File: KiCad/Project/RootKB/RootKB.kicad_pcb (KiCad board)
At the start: 2 copper layers, 137.4 x 107.4 mm, 70 parts, among them J1 OLED-128x32, SW1 Switch, U1 Arduino_Pro_Micro, U2 TRRS

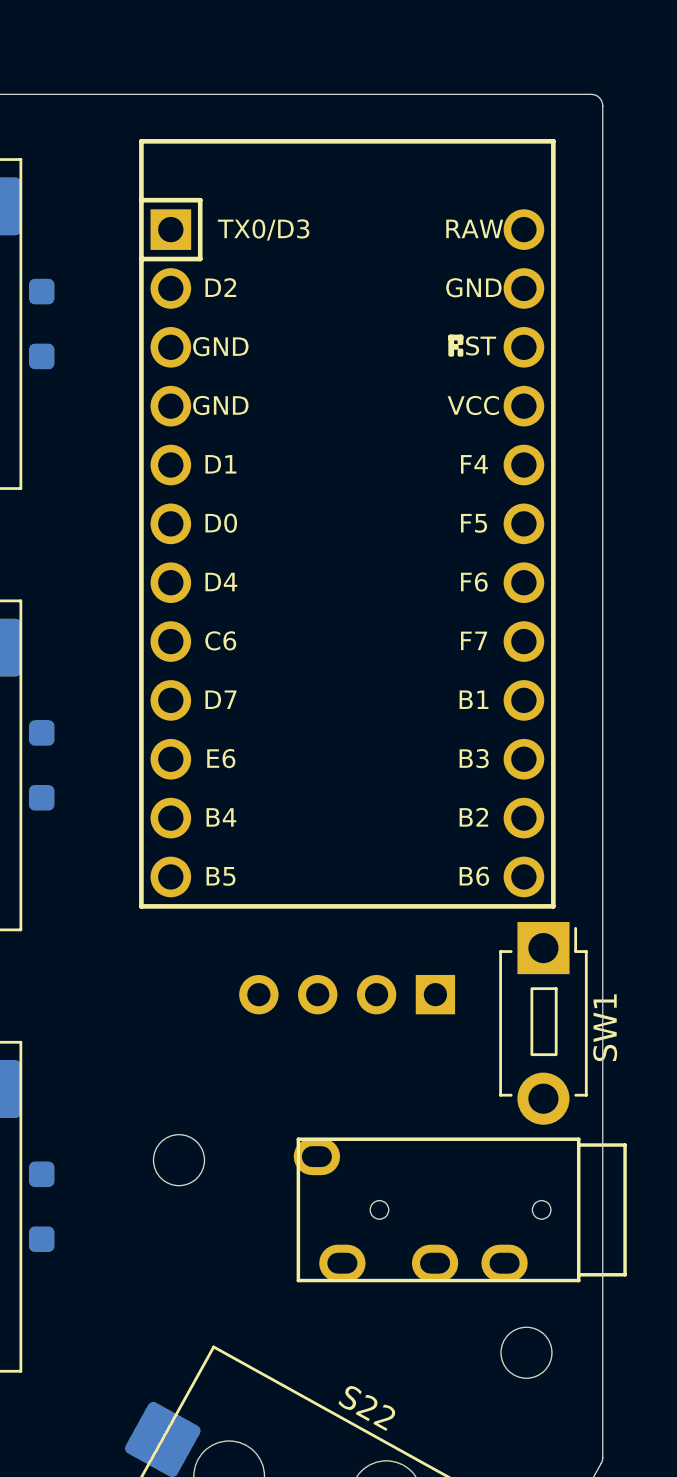
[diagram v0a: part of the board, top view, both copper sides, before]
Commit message: adjust for larger arduino pro micro (Type C)
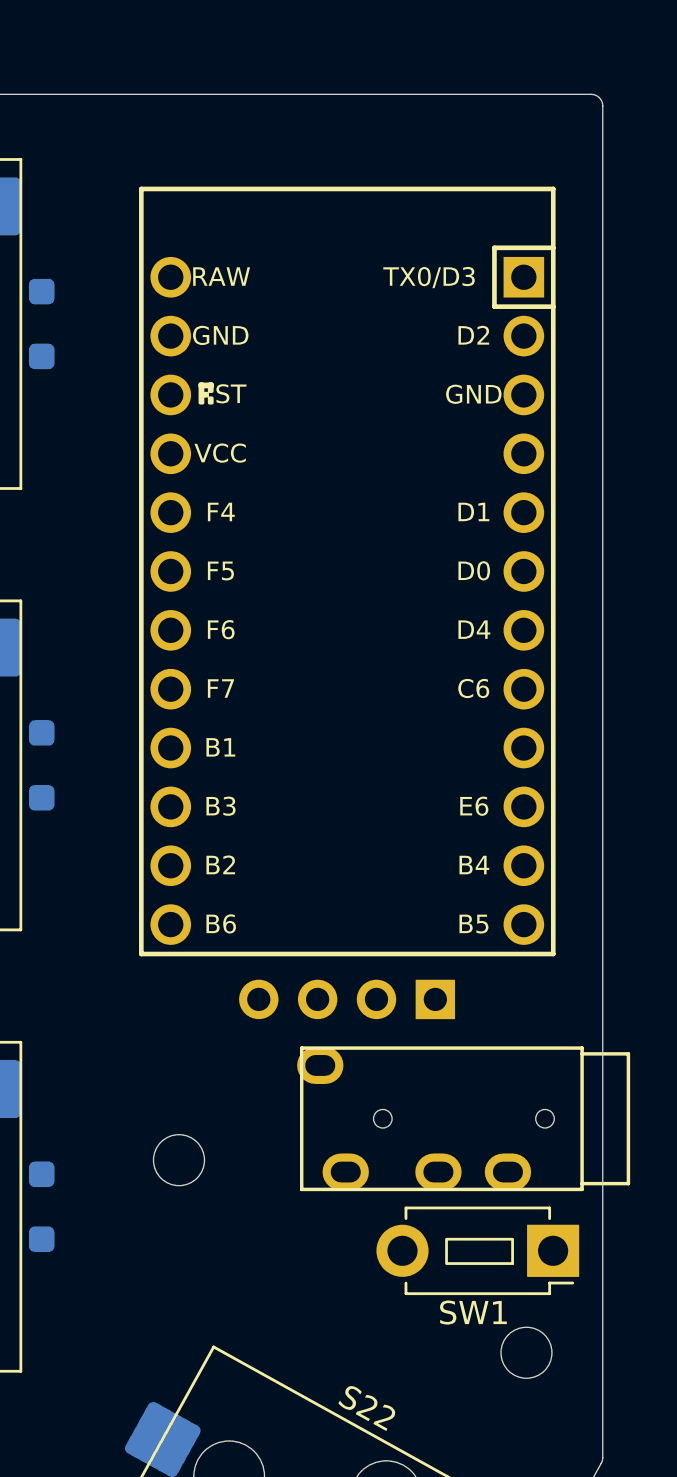
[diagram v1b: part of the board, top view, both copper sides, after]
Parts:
- U1: moved to B.Cu
- moved SW1 13.1 mm to (211.0, 101.9), turned to 180 degrees
- moved U2 3.94 mm to (212.3, 96.2)
- moved U1 2.06 mm to (202.2, 73.9), turned to 180 degrees
- moved J1 0.21 mm to (196.2, 92.7)

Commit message: add right side
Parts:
- removed the D1 at (93.7, 61.9)
- removed the D10 at (150.9, 71.4)
- removed the D11 at (169.9, 76.2)
- removed the D12 at (189.0, 81.0)
- removed the D13 at (93.7, 100.0)
- removed the D14 at (112.8, 100.0)
- removed the D15 at (131.8, 95.2)
- removed the D16 at (150.9, 90.5)
- removed the D17 at (169.9, 95.2)
- removed the D18 at (189.0, 100.0)
- removed the D19 at (161.2, 121.9)
- removed the D2 at (112.8, 61.9)
- removed the D20 at (179.1, 129.1)
- removed the D21 at (195.8, 138.2)
- removed the D22 at (206.1, 119.7)
- removed the D3 at (131.8, 57.1)
- removed the D4 at (150.9, 52.4)
- removed the D5 at (169.9, 57.1)
- removed the D6 at (189.0, 61.9)
- removed the D7 at (93.7, 81.0)
- removed the D8 at (112.8, 81.0)
- removed the D9 at (131.8, 76.2)
- removed the J1 at (196.2, 92.7)
- removed the LED1 at (85.7, 67.0)
- removed the LED10 at (142.9, 76.5)
- removed the LED11 at (161.9, 81.3)
- removed the LED12 at (181.0, 86.0)
- removed the LED13 at (85.7, 105.1)
- removed the LED14 at (104.8, 105.1)
- removed the LED15 at (123.8, 100.3)
- removed the LED16 at (142.9, 95.6)
- removed the LED17 at (161.9, 100.3)
- removed the LED18 at (181.0, 105.1)
- removed the LED19 at (151.8, 122.5)
- removed the LED2 at (104.8, 67.0)
- removed the LED20 at (169.7, 129.6)
- removed the LED21 at (186.3, 138.9)
- removed the LED22 at (196.7, 120.2)
- removed the LED3 at (123.8, 62.2)
- removed the LED4 at (142.9, 57.5)
- removed the LED5 at (161.9, 62.2)
- removed the LED6 at (181.0, 67.0)
- removed the LED7 at (85.7, 86.0)
- removed the LED8 at (104.8, 86.0)
- removed the LED9 at (123.8, 81.3)
- removed the S1 at (85.7, 61.9)
- removed the S10 at (142.9, 71.4)
- removed the S11 at (161.9, 76.2)
- removed the S12 at (181.0, 81.0)
- removed the S13 at (85.7, 100.0)
- removed the S14 at (104.8, 100.0)
- removed the S15 at (123.8, 95.2)
- removed the S16 at (142.9, 90.5)
- removed the S17 at (161.9, 95.2)
- removed the S18 at (181.0, 100.0)
- removed the S19 at (154.3, 118.1)
- removed the S2 at (104.8, 61.9)
- removed the S20 at (172.1, 125.2)
- removed the S21 at (188.8, 134.4)
- removed the S22 at (199.2, 115.7)
- removed the S3 at (123.8, 57.1)
- removed the S4 at (142.9, 52.4)
- removed the S5 at (161.9, 57.1)
- removed the S6 at (181.0, 61.9)
- removed the S7 at (85.7, 81.0)
- removed the S8 at (104.8, 81.0)
- removed the S9 at (123.8, 76.2)
- removed the SW1 at (211.0, 101.9)
- removed the U1 at (202.2, 73.9)
- removed the U2 at (212.3, 96.2)
- added D1: Diode, Diode_SMD:D_SOD-123F, B.Cu at (348.4, 105.7)
- added D1: Diode, Diode_SMD:D_SOD-123F, B.Cu at (74.9, 104.9)
- added D10: Diode, Diode_SMD:D_SOD-123F, B.Cu at (291.2, 115.2)
- added D10: Diode, Diode_SMD:D_SOD-123F, B.Cu at (132.1, 114.4)
- added D11: Diode, Diode_SMD:D_SOD-123F, B.Cu at (272.2, 120.0)
- added D11: Diode, Diode_SMD:D_SOD-123F, B.Cu at (151.1, 119.2)
- added D12: Diode, Diode_SMD:D_SOD-123F, B.Cu at (170.2, 123.9)
- added D12: Diode, Diode_SMD:D_SOD-123F, B.Cu at (253.1, 124.7)
- added D13: Diode, Diode_SMD:D_SOD-123F, B.Cu at (74.9, 143.0)
- added D13: Diode, Diode_SMD:D_SOD-123F, B.Cu at (348.4, 143.8)
- added D14: Diode, Diode_SMD:D_SOD-123F, B.Cu at (329.3, 143.8)
- added D14: Diode, Diode_SMD:D_SOD-123F, B.Cu at (94.0, 143.0)
- added D15: Diode, Diode_SMD:D_SOD-123F, B.Cu at (113.0, 138.2)
- added D15: Diode, Diode_SMD:D_SOD-123F, B.Cu at (310.3, 139.0)
- added D16: Diode, Diode_SMD:D_SOD-123F, B.Cu at (291.2, 134.2)
- added D16: Diode, Diode_SMD:D_SOD-123F, B.Cu at (132.1, 133.5)
- added D17: Diode, Diode_SMD:D_SOD-123F, B.Cu at (272.2, 139.0)
- added D17: Diode, Diode_SMD:D_SOD-123F, B.Cu at (151.1, 138.2)
- added D18: Diode, Diode_SMD:D_SOD-123F, B.Cu at (170.2, 143.0)
- added D18: Diode, Diode_SMD:D_SOD-123F, B.Cu at (253.1, 143.8)
- added D19: Diode, Diode_SMD:D_SOD-123F, B.Cu at (278.9, 157.8)
- added D19: Diode, Diode_SMD:D_SOD-123F, B.Cu at (142.4, 164.9)
- added D2: Diode, Diode_SMD:D_SOD-123F, B.Cu at (329.3, 105.7)
- added D2: Diode, Diode_SMD:D_SOD-123F, B.Cu at (94.0, 104.9)
- added D20: Diode, Diode_SMD:D_SOD-123F, B.Cu at (160.3, 172.0)
- added D20: Diode, Diode_SMD:D_SOD-123F, B.Cu at (261.0, 165.0)
- added D21: Diode, Diode_SMD:D_SOD-123F, B.Cu at (244.4, 174.1)
- added D21: Diode, Diode_SMD:D_SOD-123F, B.Cu at (177.0, 181.2)
- added D22: Diode, Diode_SMD:D_SOD-123F, B.Cu at (187.3, 162.6)
- added D22: Diode, Diode_SMD:D_SOD-123F, B.Cu at (234.0, 155.5)
- added D3: Diode, Diode_SMD:D_SOD-123F, B.Cu at (310.3, 100.9)
- added D3: Diode, Diode_SMD:D_SOD-123F, B.Cu at (113.0, 100.1)
- added D4: Diode, Diode_SMD:D_SOD-123F, B.Cu at (291.2, 96.2)
- added D4: Diode, Diode_SMD:D_SOD-123F, B.Cu at (132.1, 95.4)
- added D5: Diode, Diode_SMD:D_SOD-123F, B.Cu at (272.2, 100.9)
- added D5: Diode, Diode_SMD:D_SOD-123F, B.Cu at (151.1, 100.1)
- added D6: Diode, Diode_SMD:D_SOD-123F, B.Cu at (170.2, 104.9)
- added D6: Diode, Diode_SMD:D_SOD-123F, B.Cu at (253.1, 105.7)
- added D7: Diode, Diode_SMD:D_SOD-123F, B.Cu at (74.9, 123.9)
- added D7: Diode, Diode_SMD:D_SOD-123F, B.Cu at (348.4, 124.7)
- added D8: Diode, Diode_SMD:D_SOD-123F, B.Cu at (329.3, 124.7)
- added D8: Diode, Diode_SMD:D_SOD-123F, B.Cu at (94.0, 123.9)
- added D9: Diode, Diode_SMD:D_SOD-123F, B.Cu at (113.0, 119.2)
- added D9: Diode, Diode_SMD:D_SOD-123F, B.Cu at (310.3, 120.0)
- added J1: OLED-128x32, display:OLED-128x32-cutout, F.Cu at (217.8, 136.4)
- added J1: OLED-128x32, display:OLED-128x32-cutout, F.Cu at (177.4, 135.6)
- added LED1: MX_SK6812MINI-E, PCM_marbastlib-mx:LED_MX_6028R, B.Cu at (340.3, 110.8)
- added LED1: MX_SK6812MINI-E, PCM_marbastlib-mx:LED_MX_6028R, B.Cu at (66.9, 110.0)
- added LED10: MX_SK6812MINI-E, PCM_marbastlib-mx:LED_MX_6028R, B.Cu at (124.1, 119.5)
- added LED10: MX_SK6812MINI-E, PCM_marbastlib-mx:LED_MX_6028R, B.Cu at (283.1, 120.3)
- added LED11: MX_SK6812MINI-E, PCM_marbastlib-mx:LED_MX_6028R, B.Cu at (143.1, 124.2)
- added LED11: MX_SK6812MINI-E, PCM_marbastlib-mx:LED_MX_6028R, B.Cu at (264.1, 125.0)
- added LED12: MX_SK6812MINI-E, PCM_marbastlib-mx:LED_MX_6028R, B.Cu at (162.2, 129.0)
- added LED12: MX_SK6812MINI-E, PCM_marbastlib-mx:LED_MX_6028R, B.Cu at (245.0, 129.8)
- added LED13: MX_SK6812MINI-E, PCM_marbastlib-mx:LED_MX_6028R, B.Cu at (66.9, 148.1)
- added LED13: MX_SK6812MINI-E, PCM_marbastlib-mx:LED_MX_6028R, B.Cu at (340.3, 148.9)
- added LED14: MX_SK6812MINI-E, PCM_marbastlib-mx:LED_MX_6028R, B.Cu at (321.2, 148.9)
- added LED14: MX_SK6812MINI-E, PCM_marbastlib-mx:LED_MX_6028R, B.Cu at (86.0, 148.1)
- added LED15: MX_SK6812MINI-E, PCM_marbastlib-mx:LED_MX_6028R, B.Cu at (105.0, 143.3)
- added LED15: MX_SK6812MINI-E, PCM_marbastlib-mx:LED_MX_6028R, B.Cu at (302.2, 144.1)
- added LED16: MX_SK6812MINI-E, PCM_marbastlib-mx:LED_MX_6028R, B.Cu at (124.1, 138.5)
- added LED16: MX_SK6812MINI-E, PCM_marbastlib-mx:LED_MX_6028R, B.Cu at (283.1, 139.3)
- added LED17: MX_SK6812MINI-E, PCM_marbastlib-mx:LED_MX_6028R, B.Cu at (264.1, 144.1)
- added LED17: MX_SK6812MINI-E, PCM_marbastlib-mx:LED_MX_6028R, B.Cu at (143.1, 143.3)
- added LED18: MX_SK6812MINI-E, PCM_marbastlib-mx:LED_MX_6028R, B.Cu at (245.0, 148.9)
- added LED18: MX_SK6812MINI-E, PCM_marbastlib-mx:LED_MX_6028R, B.Cu at (162.2, 148.1)
- added LED19: MX_SK6812MINI-E, PCM_marbastlib-mx:LED_MX_6028R, B.Cu at (133.1, 165.5)
- added LED19: MX_SK6812MINI-E, PCM_marbastlib-mx:LED_MX_6028R, B.Cu at (274.2, 166.3)
- added LED2: MX_SK6812MINI-E, PCM_marbastlib-mx:LED_MX_6028R, B.Cu at (321.2, 110.8)
- added LED2: MX_SK6812MINI-E, PCM_marbastlib-mx:LED_MX_6028R, B.Cu at (86.0, 110.0)
- added LED20: MX_SK6812MINI-E, PCM_marbastlib-mx:LED_MX_6028R, B.Cu at (150.9, 172.6)
- added LED20: MX_SK6812MINI-E, PCM_marbastlib-mx:LED_MX_6028R, B.Cu at (256.3, 173.4)
- added LED21: MX_SK6812MINI-E, PCM_marbastlib-mx:LED_MX_6028R, B.Cu at (239.7, 182.6)
- added LED21: MX_SK6812MINI-E, PCM_marbastlib-mx:LED_MX_6028R, B.Cu at (167.5, 181.8)
- added LED22: MX_SK6812MINI-E, PCM_marbastlib-mx:LED_MX_6028R, B.Cu at (177.9, 163.1)
- added LED22: MX_SK6812MINI-E, PCM_marbastlib-mx:LED_MX_6028R, B.Cu at (229.3, 163.9)
- added LED3: MX_SK6812MINI-E, PCM_marbastlib-mx:LED_MX_6028R, B.Cu at (302.2, 106.0)
- added LED3: MX_SK6812MINI-E, PCM_marbastlib-mx:LED_MX_6028R, B.Cu at (105.0, 105.2)
- added LED4: MX_SK6812MINI-E, PCM_marbastlib-mx:LED_MX_6028R, B.Cu at (124.1, 100.4)
- added LED4: MX_SK6812MINI-E, PCM_marbastlib-mx:LED_MX_6028R, B.Cu at (283.1, 101.2)
- added LED5: MX_SK6812MINI-E, PCM_marbastlib-mx:LED_MX_6028R, B.Cu at (143.1, 105.2)
- added LED5: MX_SK6812MINI-E, PCM_marbastlib-mx:LED_MX_6028R, B.Cu at (264.1, 106.0)
- added LED6: MX_SK6812MINI-E, PCM_marbastlib-mx:LED_MX_6028R, B.Cu at (245.0, 110.8)
- added LED6: MX_SK6812MINI-E, PCM_marbastlib-mx:LED_MX_6028R, B.Cu at (162.2, 110.0)
- added LED7: MX_SK6812MINI-E, PCM_marbastlib-mx:LED_MX_6028R, B.Cu at (340.3, 129.8)
- added LED7: MX_SK6812MINI-E, PCM_marbastlib-mx:LED_MX_6028R, B.Cu at (66.9, 129.0)
- added LED8: MX_SK6812MINI-E, PCM_marbastlib-mx:LED_MX_6028R, B.Cu at (86.0, 129.0)
- added LED8: MX_SK6812MINI-E, PCM_marbastlib-mx:LED_MX_6028R, B.Cu at (321.2, 129.8)
- added LED9: MX_SK6812MINI-E, PCM_marbastlib-mx:LED_MX_6028R, B.Cu at (302.2, 125.0)
- added LED9: MX_SK6812MINI-E, PCM_marbastlib-mx:LED_MX_6028R, B.Cu at (105.0, 124.2)
- added S1: Keyswitch, PCM_Switch_Keyboard_Hotswap_Kailh:SW_Hotswap_Kailh_MX_1.00u, F.Cu at (66.9, 104.9)
- added S1: Keyswitch, PCM_Switch_Keyboard_Hotswap_Kailh:SW_Hotswap_Kailh_MX_1.00u, F.Cu at (340.3, 105.7)
- added S10: Keyswitch, PCM_Switch_Keyboard_Hotswap_Kailh:SW_Hotswap_Kailh_MX_1.00u, F.Cu at (283.1, 115.2)
- added S10: Keyswitch, PCM_Switch_Keyboard_Hotswap_Kailh:SW_Hotswap_Kailh_MX_1.00u, F.Cu at (124.1, 114.4)
- added S11: Keyswitch, PCM_Switch_Keyboard_Hotswap_Kailh:SW_Hotswap_Kailh_MX_1.00u, F.Cu at (264.1, 120.0)
- added S11: Keyswitch, PCM_Switch_Keyboard_Hotswap_Kailh:SW_Hotswap_Kailh_MX_1.00u, F.Cu at (143.1, 119.2)
- added S12: Keyswitch, PCM_Switch_Keyboard_Hotswap_Kailh:SW_Hotswap_Kailh_MX_1.00u, F.Cu at (245.0, 124.7)
- added S12: Keyswitch, PCM_Switch_Keyboard_Hotswap_Kailh:SW_Hotswap_Kailh_MX_1.00u, F.Cu at (162.2, 123.9)
- added S13: Keyswitch, PCM_Switch_Keyboard_Hotswap_Kailh:SW_Hotswap_Kailh_MX_1.00u, F.Cu at (66.9, 143.0)
- added S13: Keyswitch, PCM_Switch_Keyboard_Hotswap_Kailh:SW_Hotswap_Kailh_MX_1.00u, F.Cu at (340.3, 143.8)
- added S14: Keyswitch, PCM_Switch_Keyboard_Hotswap_Kailh:SW_Hotswap_Kailh_MX_1.00u, F.Cu at (321.2, 143.8)
- added S14: Keyswitch, PCM_Switch_Keyboard_Hotswap_Kailh:SW_Hotswap_Kailh_MX_1.00u, F.Cu at (86.0, 143.0)
- added S15: Keyswitch, PCM_Switch_Keyboard_Hotswap_Kailh:SW_Hotswap_Kailh_MX_1.00u, F.Cu at (105.0, 138.2)
- added S15: Keyswitch, PCM_Switch_Keyboard_Hotswap_Kailh:SW_Hotswap_Kailh_MX_1.00u, F.Cu at (302.2, 139.0)
- added S16: Keyswitch, PCM_Switch_Keyboard_Hotswap_Kailh:SW_Hotswap_Kailh_MX_1.00u, F.Cu at (283.1, 134.2)
- added S16: Keyswitch, PCM_Switch_Keyboard_Hotswap_Kailh:SW_Hotswap_Kailh_MX_1.00u, F.Cu at (124.1, 133.5)
- added S17: Keyswitch, PCM_Switch_Keyboard_Hotswap_Kailh:SW_Hotswap_Kailh_MX_1.00u, F.Cu at (143.1, 138.2)
- added S17: Keyswitch, PCM_Switch_Keyboard_Hotswap_Kailh:SW_Hotswap_Kailh_MX_1.00u, F.Cu at (264.1, 139.0)
- added S18: Keyswitch, PCM_Switch_Keyboard_Hotswap_Kailh:SW_Hotswap_Kailh_MX_1.00u, F.Cu at (245.0, 143.8)
- added S18: Keyswitch, PCM_Switch_Keyboard_Hotswap_Kailh:SW_Hotswap_Kailh_MX_1.00u, F.Cu at (162.2, 143.0)
- added S19: Keyswitch, PCM_Switch_Keyboard_Hotswap_Kailh:SW_Hotswap_Kailh_MX_1.00u, F.Cu at (271.7, 161.8)
- added S19: Keyswitch, PCM_Switch_Keyboard_Hotswap_Kailh:SW_Hotswap_Kailh_MX_1.00u, F.Cu at (135.5, 161.0)
- added S2: Keyswitch, PCM_Switch_Keyboard_Hotswap_Kailh:SW_Hotswap_Kailh_MX_1.00u, F.Cu at (321.2, 105.7)
- added S2: Keyswitch, PCM_Switch_Keyboard_Hotswap_Kailh:SW_Hotswap_Kailh_MX_1.00u, F.Cu at (86.0, 104.9)
- added S20: Keyswitch, PCM_Switch_Keyboard_Hotswap_Kailh:SW_Hotswap_Kailh_MX_1.25u_90deg, F.Cu at (253.9, 169.0)
- added S20: Keyswitch, PCM_Switch_Keyboard_Hotswap_Kailh:SW_Hotswap_Kailh_MX_1.25u_90deg, F.Cu at (153.3, 168.2)
- added S21: Keyswitch, PCM_Switch_Keyboard_Hotswap_Kailh:SW_Hotswap_Kailh_MX_1.25u_90deg, F.Cu at (237.2, 178.2)
- added S21: Keyswitch, PCM_Switch_Keyboard_Hotswap_Kailh:SW_Hotswap_Kailh_MX_1.25u_90deg, F.Cu at (170.0, 177.4)
- added S22: Keyswitch, PCM_Switch_Keyboard_Hotswap_Kailh:SW_Hotswap_Kailh_MX_1.00u, F.Cu at (226.8, 159.5)
- added S22: Keyswitch, PCM_Switch_Keyboard_Hotswap_Kailh:SW_Hotswap_Kailh_MX_1.00u, F.Cu at (180.4, 158.7)
- added S3: Keyswitch, PCM_Switch_Keyboard_Hotswap_Kailh:SW_Hotswap_Kailh_MX_1.00u, F.Cu at (302.2, 100.9)
- added S3: Keyswitch, PCM_Switch_Keyboard_Hotswap_Kailh:SW_Hotswap_Kailh_MX_1.00u, F.Cu at (105.0, 100.1)
- added S4: Keyswitch, PCM_Switch_Keyboard_Hotswap_Kailh:SW_Hotswap_Kailh_MX_1.00u, F.Cu at (124.1, 95.4)
- added S4: Keyswitch, PCM_Switch_Keyboard_Hotswap_Kailh:SW_Hotswap_Kailh_MX_1.00u, F.Cu at (283.1, 96.2)
- added S5: Keyswitch, PCM_Switch_Keyboard_Hotswap_Kailh:SW_Hotswap_Kailh_MX_1.00u, F.Cu at (264.1, 100.9)
- added S5: Keyswitch, PCM_Switch_Keyboard_Hotswap_Kailh:SW_Hotswap_Kailh_MX_1.00u, F.Cu at (143.1, 100.1)
- added S6: Keyswitch, PCM_Switch_Keyboard_Hotswap_Kailh:SW_Hotswap_Kailh_MX_1.00u, F.Cu at (245.0, 105.7)
- added S6: Keyswitch, PCM_Switch_Keyboard_Hotswap_Kailh:SW_Hotswap_Kailh_MX_1.00u, F.Cu at (162.2, 104.9)
- added S7: Keyswitch, PCM_Switch_Keyboard_Hotswap_Kailh:SW_Hotswap_Kailh_MX_1.00u, F.Cu at (340.3, 124.7)
- added S7: Keyswitch, PCM_Switch_Keyboard_Hotswap_Kailh:SW_Hotswap_Kailh_MX_1.00u, F.Cu at (66.9, 123.9)
- added S8: Keyswitch, PCM_Switch_Keyboard_Hotswap_Kailh:SW_Hotswap_Kailh_MX_1.00u, F.Cu at (86.0, 123.9)
- added S8: Keyswitch, PCM_Switch_Keyboard_Hotswap_Kailh:SW_Hotswap_Kailh_MX_1.00u, F.Cu at (321.2, 124.7)
- added S9: Keyswitch, PCM_Switch_Keyboard_Hotswap_Kailh:SW_Hotswap_Kailh_MX_1.00u, F.Cu at (105.0, 119.2)
- added S9: Keyswitch, PCM_Switch_Keyboard_Hotswap_Kailh:SW_Hotswap_Kailh_MX_1.00u, F.Cu at (302.2, 120.0)
- added SW1: Switch, ScottoKeebs_Components:Button_MJTP1250, F.Cu at (215.0, 145.7)
- added SW1: Switch, ScottoKeebs_Components:Button_MJTP1250, F.Cu at (192.3, 144.9)
- added U1: Arduino_Pro_Micro, ScottoKeebs_MCU:Arduino_Pro_Micro, B.Cu at (183.4, 116.8)
- added U1: Arduino_Pro_Micro, ScottoKeebs_MCU:Arduino_Pro_Micro, B.Cu at (223.8, 117.6)
- added U2: TRRS, ScottoKeebs_Components:TRRS_PJ-320A, F.Cu at (213.7, 140.0)
- added U2: TRRS, ScottoKeebs_Components:TRRS_PJ-320A, F.Cu at (193.5, 139.2)
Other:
- board size 137.4 x 107.4 mm -> 293.3 x 108.2 mm
